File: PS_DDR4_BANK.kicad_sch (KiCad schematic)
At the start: 1 part, among them U13 XCZU15EG-2FFVB1156E

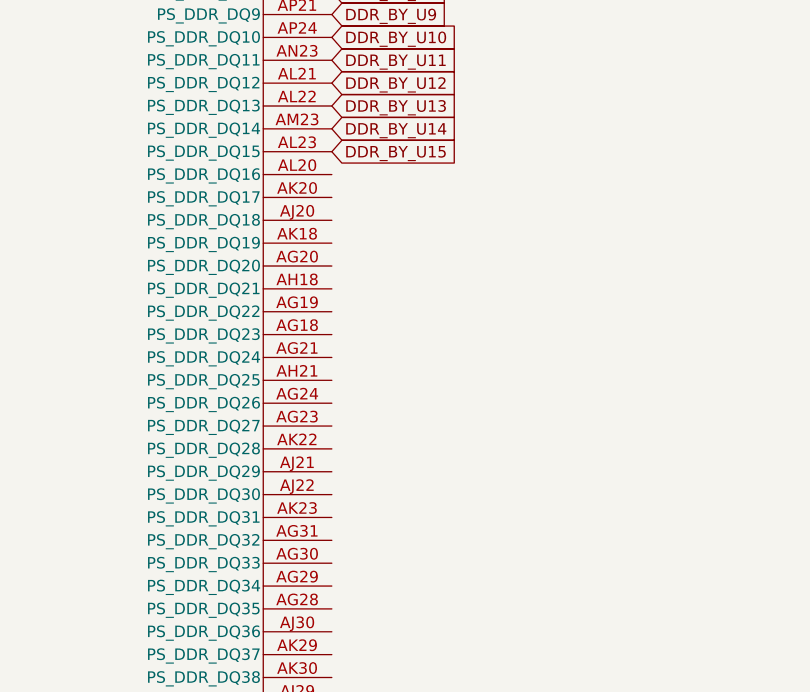
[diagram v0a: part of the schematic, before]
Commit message: DDR4 data lines
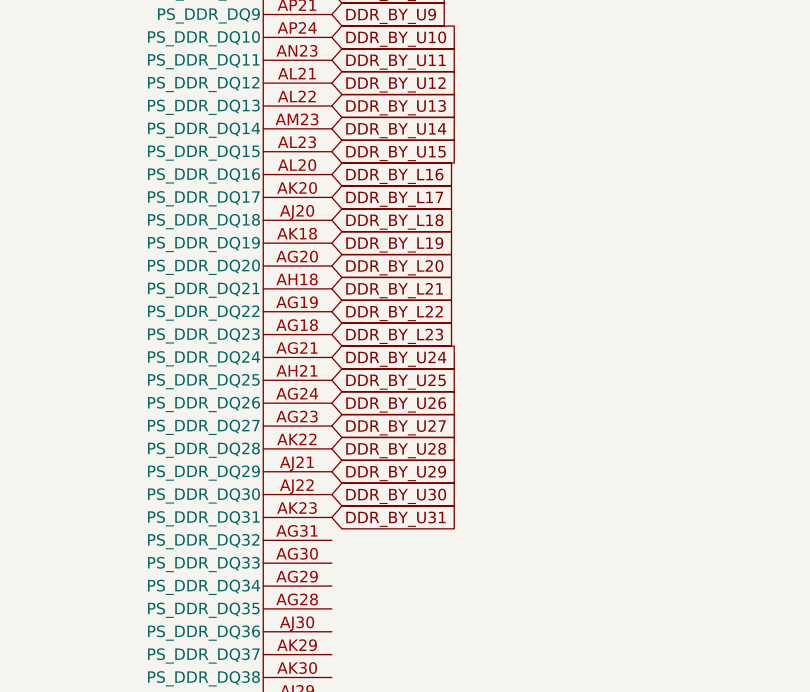
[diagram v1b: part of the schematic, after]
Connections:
- net DDR_BY_L23: now reaches U13.AG18 (PS_DDR_DQ23)
- net DDR_BY_L22: now reaches U13.AG19 (PS_DDR_DQ22)
- net DDR_BY_L20: now reaches U13.AG20 (PS_DDR_DQ20)
- net DDR_BY_U24: now reaches U13.AG21 (PS_DDR_DQ24)
- net DDR_BY_U27: now reaches U13.AG23 (PS_DDR_DQ27)
- net DDR_BY_U26: now reaches U13.AG24 (PS_DDR_DQ26)
- net DDR_BY_L21: now reaches U13.AH18 (PS_DDR_DQ21)
- net DDR_BY_U25: now reaches U13.AH21 (PS_DDR_DQ25)
- net DDR_BY_L18: now reaches U13.AJ20 (PS_DDR_DQ18)
- net DDR_BY_U29: now reaches U13.AJ21 (PS_DDR_DQ29)
- net DDR_BY_U30: now reaches U13.AJ22 (PS_DDR_DQ30)
- net DDR_BY_L19: now reaches U13.AK18 (PS_DDR_DQ19)
- net DDR_BY_L17: now reaches U13.AK20 (PS_DDR_DQ17)
- net DDR_BY_U28: now reaches U13.AK22 (PS_DDR_DQ28)
- net DDR_BY_U31: now reaches U13.AK23 (PS_DDR_DQ31)
- net DDR_BY_L16: now reaches U13.AL20 (PS_DDR_DQ16)
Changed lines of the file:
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@@
 (kicad_sch (version 20230121) (generator eeschema)
   (paper "A4")
+  (global_label "DDR_BY_U31" (shape input) (at 95.25 111.76 0) (fields_autoplaced)
+    (effects (font (size 1.27 1.27)) (justify left))
+    (property "Intersheetrefs" "${INTERSHEET_REFS}" (at 110.0091 111.76 0)
+      (effects (font (size 1.27 1.27)) (justify left) hide)
+    )
+  )
   (global_label "DDR_A13" (shape input) (at 259.08 60.96 0) (fields_autoplaced)
     (effects (font (size 1.27 1.27)) (justify left))
@@
     )
   )
+  (global_label "DDR_BY_U27" (shape input) (at 95.25 101.6 0) (fields_autoplaced)
+    (effects (font (size 1.27 1.27)) (justify left))
+    (property "Intersheetrefs" "${INTERSHEET_REFS}" (at 110.0091 101.6 0)
+      (effects (font (size 1.27 1.27)) (justify left) hide)
+    )
+  )
   (global_label "DDR_A16" (shape input) (at 259.08 68.58 0) (fields_autoplaced)
     (effects (font (size 1.27 1.27)) (justify left))
@@
     )
   )
+  (global_label "DDR_BY_L17" (shape input) (at 95.25 76.2 0) (fields_autoplaced)
+    (effects (font (size 1.27 1.27)) (justify left))
+    (property "Intersheetrefs" "${INTERSHEET_REFS}" (at 109.7067 76.2 0)
+      (effects (font (size 1.27 1.27)) (justify left) hide)
+    )
+  )
+  (global_label "DDR_BY_L19" (shape input) (at 95.25 81.28 0) (fields_autoplaced)
+    (effects (font (size 1.27 1.27)) (justify left))
+    (property "Intersheetrefs" "${INTERSHEET_REFS}" (at 109.7067 81.28 0)
+      (effects (font (size 1.27 1.27)) (justify left) hide)
+    )
+  )
   (global_label "DDR_CK-" (shape input) (at 259.08 86.36 0) (fields_autoplaced)
     (effects (font (size 1.27 1.27)) (justify left))
@@
     )
   )
+  (global_label "DDR_BY_U28" (shape input) (at 95.25 104.14 0) (fields_autoplaced)
+    (effects (font (size 1.27 1.27)) (justify left))
+    (property "Intersheetrefs" "${INTERSHEET_REFS}" (at 110.0091 104.14 0)
+      (effects (font (size 1.27 1.27)) (justify left) hide)
+    )
+  )
   (global_label "DDR_BY_U12" (shape input) (at 95.25 63.5 0) (fields_autoplaced)
     (effects (font (size 1.27 1.27)) (justify left))
@@
     )
   )
+  (global_label "DDR_BY_L16" (shape input) (at 95.25 73.66 0) (fields_autoplaced)
+    (effects (font (size 1.27 1.27)) (justify left))
+    (property "Intersheetrefs" "${INTERSHEET_REFS}" (at 109.7067 73.66 0)
+      (effects (font (size 1.27 1.27)) (justify left) hide)
+    )
+  )
   (global_label "DDR_BY_L0" (shape input) (at 95.25 33.02 0) (fields_autoplaced)
     (effects (font (size 1.27 1.27)) (justify left))
@@
     )
   )
+  (global_label "DDR_BY_U24" (shape input) (at 95.25 93.98 0) (fields_autoplaced)
+    (effects (font (size 1.27 1.27)) (justify left))
+    (property "Intersheetrefs" "${INTERSHEET_REFS}" (at 110.0091 93.98 0)
+      (effects (font (size 1.27 1.27)) (justify left) hide)
+    )
+  )
   (global_label "DDR_A5" (shape input) (at 259.08 40.64 0) (fields_autoplaced)
     (effects (font (size 1.27 1.27)) (justify left))
@@
     (effects (font (size 1.27 1.27)) (justify left))
     (property "Intersheetrefs" "${INTERSHEET_REFS}" (at 270.5129 81.28 0)
+      (effects (font (size 1.27 1.27)) (justify left) hide)
+    )
+  )
+  (global_label "DDR_BY_U25" (shape input) (at 95.25 96.52 0) (fields_autoplaced)
+    (effects (font (size 1.27 1.27)) (justify left))
+    (property "Intersheetrefs" "${INTERSHEET_REFS}" (at 110.0091 96.52 0)
+      (effects (font (size 1.27 1.27)) (justify left) hide)
+    )
+  )
+  (global_label "DDR_BY_U30" (shape input) (at 95.25 109.22 0) (fields_autoplaced)
+    (effects (font (size 1.27 1.27)) (justify left))
+    (property "Intersheetrefs" "${INTERSHEET_REFS}" (at 110.0091 109.22 0)
       (effects (font (size 1.27 1.27)) (justify left) hide)
     )
@@
     )
   )
+  (global_label "DDR_BY_L22" (shape input) (at 95.25 88.9 0) (fields_autoplaced)
+    (effects (font (size 1.27 1.27)) (justify left))
+    (property "Intersheetrefs" "${INTERSHEET_REFS}" (at 109.7067 88.9 0)
+      (effects (font (size 1.27 1.27)) (justify left) hide)
+    )
+  )
   (global_label "DDR_BY_L4" (shape input) (at 95.25 43.18 0) (fields_autoplaced)
     (effects (font (size 1.27 1.27)) (justify left))
@@
     )
   )
+  (global_label "DDR_BY_U26" (shape input) (at 95.25 99.06 0) (fields_autoplaced)
+    (effects (font (size 1.27 1.27)) (justify left))
+    (property "Intersheetrefs" "${INTERSHEET_REFS}" (at 110.0091 99.06 0)
+      (effects (font (size 1.27 1.27)) (justify left) hide)
+    )
+  )
   (global_label "DDR_A1" (shape input) (at 259.08 30.48 0) (fields_autoplaced)
     (effects (font (size 1.27 1.27)) (justify left))
@@
     )
   )
+  (global_label "DDR_BY_L21" (shape input) (at 95.25 86.36 0) (fields_autoplaced)
+    (effects (font (size 1.27 1.27)) (justify left))
+    (property "Intersheetrefs" "${INTERSHEET_REFS}" (at 109.7067 86.36 0)
+      (effects (font (size 1.27 1.27)) (justify left) hide)
+    )
+  )
+  (global_label "DDR_BY_L20" (shape input) (at 95.25 83.82 0) (fields_autoplaced)
+    (effects (font (size 1.27 1.27)) (justify left))
+    (property "Intersheetrefs" "${INTERSHEET_REFS}" (at 109.7067 83.82 0)
+      (effects (font (size 1.27 1.27)) (justify left) hide)
+    )
+  )
+  (global_label "DDR_BY_U29" (shape input) (at 95.25 106.68 0) (fields_autoplaced)
+    (effects (font (size 1.27 1.27)) (justify left))
+    (property "Intersheetrefs" "${INTERSHEET_REFS}" (at 110.0091 106.68 0)
+      (effects (font (size 1.27 1.27)) (justify left) hide)
+    )
+  )
+  (global_label "DDR_BY_L18" (shape input) (at 95.25 78.74 0) (fields_autoplaced)
+    (effects (font (size 1.27 1.27)) (justify left))
+    (property "Intersheetrefs" "${INTERSHEET_REFS}" (at 109.7067 78.74 0)
+      (effects (font (size 1.27 1.27)) (justify left) hide)
+    )
+  )
   (global_label "DDR_A4" (shape input) (at 259.08 38.1 0) (fields_autoplaced)
     (effects (font (size 1.27 1.27)) (justify left))
@@
       (effects (font (size 1.27 1.27)) (justify left) hide)
     )
+  )
+  (global_label "DDR_BY_L23" (shape input) (at 95.25 91.44 0) (fields_autoplaced)
+    (effects (font (size 1.27 1.27)) (justify left))
+    (property "Intersheetrefs" "${INTERSHEET_REFS}" (at 109.7067 91.44 0)
+      (effects (font (size 1.27 1.27)) (justify left) hide)
+    )
